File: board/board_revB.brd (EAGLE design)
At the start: 94 x 44.5 mm, 84 parts, among them Q1 ULN2003AS, Q2 ULN2003AD, Y1 8Mhz

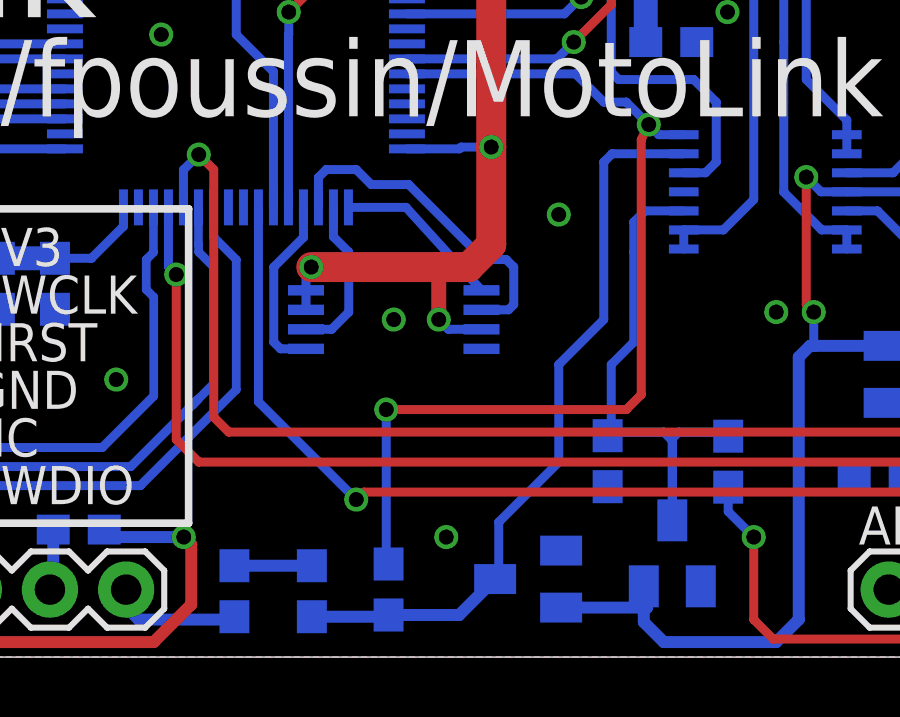
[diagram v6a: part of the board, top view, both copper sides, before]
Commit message: [GUI] Working on XML file saving
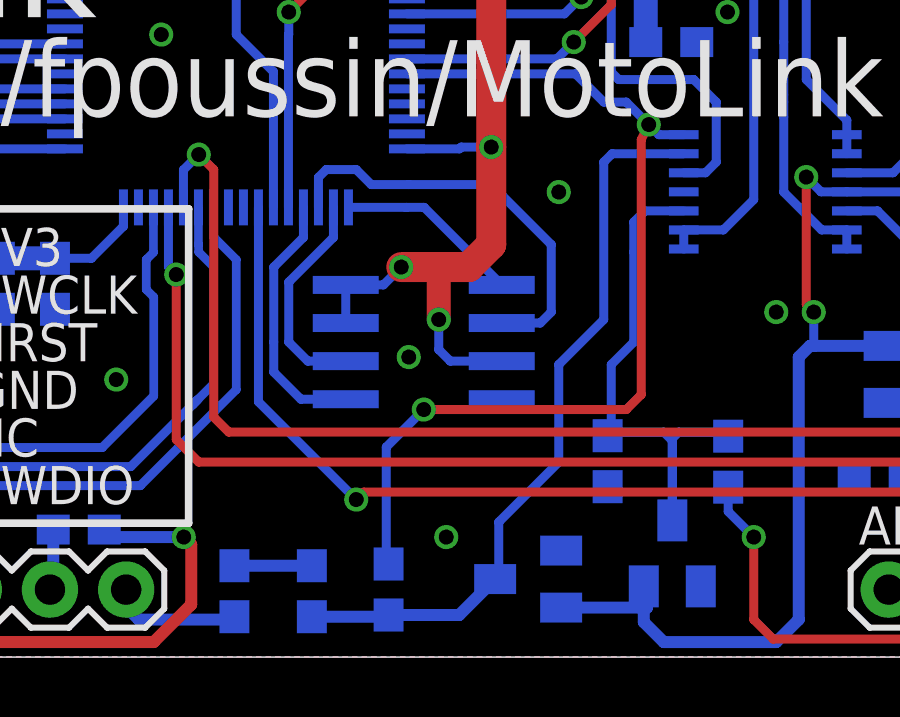
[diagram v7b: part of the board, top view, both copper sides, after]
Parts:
- IC_EE: value 25LC040ST -> 25LC080SN; device microchip:TSSOP8 -> microchip:SO-08
- moved IC_EE 1.25 mm to (48.5, 10.5)
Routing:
- net SPI2_MOSI: track 6.07 -> 8.67 mm
- net SPI2_MISO: track 11.4 -> 14.0 mm
- net SPI2_SCK: track 5.36 -> 7.27 mm
- net AN_KNOCK: track 33.0 -> 32.3 mm
- net +3V3: track 360.5 -> 361.1 mm
- net SPI2_NSS: track 5.66 -> 6.18 mm
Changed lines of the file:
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@@
 <?xml version="1.0" encoding="utf-8"?>
 <!DOCTYPE eagle SYSTEM "eagle.dtd">
-<eagle version="7.0.0">
+<eagle version="7.1.0">
 <drawing>
 <settings>
@@
 <attribute name="VALUE" x="84.75" y="38.025" size="1.016" layer="28" rot="MR0"/>
 </element>
-<element name="IC_EE" library="microchip" package="TSSOP8" value="25LC040ST" x="47.5" y="11.25" smashed="yes" rot="MR270">
-<attribute name="OC_NEWARK" value="72J3684" x="47.5" y="11.25" size="1.778" layer="28" font="vector" ratio="15" rot="MR270" display="off"/>
-<attribute name="MPN" value="25LC040A-I/ST" x="47.5" y="11.25" size="1.778" layer="28" font="vector" ratio="15" rot="MR270" display="off"/>
-<attribute name="MF" value="MICROCHIP" x="47.5" y="11.25" size="1.778" layer="28" font="vector" ratio="15" rot="MR270" display="off"/>
-<attribute name="OC_FARNELL" value="1815998" x="47.5" y="11.25" size="1.778" layer="28" font="vector" ratio="15" rot="MR270" display="off"/>
-<attribute name="NAME" x="50.425" y="12.875" size="1.27" layer="26" font="vector" ratio="16" rot="MR0"/>
-<attribute name="VALUE" x="50.75" y="8.325" size="1.27" layer="28" rot="MR0"/>
+<element name="IC_EE" library="microchip" package="SO-08" value="25LC080SN" x="48.5" y="10.5" smashed="yes" rot="MR270">
+<attribute name="OC_NEWARK" value="96K4092" x="48.5" y="10.5" size="1.778" layer="28" rot="MR270" display="off"/>
+<attribute name="MPN" value="25LC080/SN" x="48.5" y="10.5" size="1.778" layer="28" rot="MR270" display="off"/>
+<attribute name="MF" value="MICROCHIP" x="48.5" y="10.5" size="1.778" layer="28" rot="MR270" display="off"/>
+<attribute name="OC_FARNELL" value="1137302" x="48.5" y="10.5" size="1.778" layer="28" rot="MR270" display="off"/>
+<attribute name="NAME" x="51.405" y="13.417" size="1.27" layer="26" font="vector" ratio="16" rot="MR0"/>
+<attribute name="VALUE" x="50.405" y="6.563" size="1.27" layer="28" rot="MR0"/>
 </element>
 </elements>
@@
 <contactref element="C6" pad="2"/>
 <contactref element="C8" pad="1"/>
-<via x="53" y="14.75" extent="1-16" drill="0.5"/>
+<via x="53" y="15.5" extent="1-16" drill="0.5"/>
 <via x="39.75" y="20.75" extent="1-16" drill="0.5"/>
 <via x="11.5" y="39.5" extent="1-16" drill="0.5"/>
 <via x="19" y="6" extent="1-16" drill="0.5"/>
 <via x="38.25" y="9.25" extent="1-16" drill="0.5"/>
-<via x="47.5" y="11.25" extent="1-16" drill="0.5"/>
+<via x="48" y="10" extent="1-16" drill="0.5"/>
 <via x="60.25" y="11.5" extent="1-16" drill="0.5"/>
 <via x="82.75" y="3.5" extent="1-16" drill="0.5"/>
@@
 <via x="58.625" y="21.5" extent="1-16" drill="0.5"/>
 <contactref element="CON_USB" pad="4"/>
-<contactref element="IC_EE" pad="4"/>
 <via x="1.75" y="24.5" extent="1-16" drill="0.5"/>
 <via x="1" y="16.5" extent="1-16" drill="0.5"/>
 <via x="4.25" y="33.25" extent="1-16" drill="0.5"/>
+<contactref element="IC_EE" pad="4"/>
 </signal>
 <signal name="+3V3">
@@
 <wire x1="92.5" y1="26" x2="90.4525" y2="26" width="0.4" layer="16"/>
 <wire x1="90.4525" y1="26" x2="90.17" y2="25.7175" width="0.4" layer="16"/>
-<contactref element="IC_EE" pad="8"/>
 <wire x1="50.9" y1="16.85" x2="50.75" y2="17" width="0.3" layer="16"/>
-<wire x1="44.575" y1="12.225" x2="44.575" y2="12.825" width="0.3" layer="16"/>
-<wire x1="44.575" y1="12.825" x2="44.75" y2="13" width="0.3" layer="16"/>
-<via x="44.75" y="13" extent="1-16" drill="0.5"/>
+<via x="47.75" y="13" extent="1-16" drill="0.5"/>
 <wire x1="50.75" y1="17" x2="50.75" y2="13.75" width="1" layer="1"/>
 <wire x1="50.75" y1="13.75" x2="50" y2="13" width="1" layer="1"/>
 <wire x1="50" y1="13" x2="49" y2="13" width="1" layer="1"/>
+<wire x1="49" y1="13" x2="47.75" y2="13" width="1" layer="1"/>
+<via x="49" y="11.25" extent="1-16" drill="0.5"/>
+<wire x1="49" y1="11.25" x2="49" y2="13" width="0.8" layer="1"/>
+<contactref element="IC_EE" pad="7"/>
+<contactref element="IC_EE" pad="8"/>
 <contactref element="IC_EE" pad="3"/>
-<wire x1="49" y1="13" x2="44.75" y2="13" width="1" layer="1"/>
-<wire x1="50.425" y1="10.925" x2="49.325" y2="10.925" width="0.3" layer="16"/>
-<wire x1="49.325" y1="10.925" x2="49" y2="11.25" width="0.3" layer="16"/>
-<via x="49" y="11.25" extent="1-16" drill="0.5"/>
-<wire x1="49" y1="11.25" x2="49" y2="13" width="0.5" layer="1"/>
-<contactref element="IC_EE" pad="7"/>
-<wire x1="44.575" y1="12.225" x2="44.575" y2="11.575" width="0.3" layer="16"/>
+<wire x1="45.9" y1="11.135" x2="45.9" y2="12.405" width="0.3" layer="16"/>
+<wire x1="51.1" y1="9.865" x2="49.385" y2="9.865" width="0.3" layer="16"/>
+<wire x1="49.385" y1="9.865" x2="49" y2="10.25" width="0.3" layer="16"/>
+<wire x1="49" y1="10.25" x2="49" y2="11.25" width="0.3" layer="16"/>
+<wire x1="45.9" y1="12.405" x2="47.155" y2="12.405" width="0.3" layer="16"/>
+<wire x1="47.155" y1="12.405" x2="47.75" y2="13" width="0.3" layer="16"/>
 </signal>
 <signal name="+12V">
@@
 <contactref element="R5" pad="1"/>
 <wire x1="47.25" y1="3.18" x2="47.3275" y2="3.1025" width="0.3" layer="16"/>
-<wire x1="47.25" y1="3.18" x2="47.25" y2="8.25" width="0.3" layer="16"/>
-<via x="47.25" y="8.25" extent="1-16" drill="0.5"/>
-<wire x1="47.25" y1="8.25" x2="55.25" y2="8.25" width="0.3" layer="1"/>
+<via x="48.5" y="8.25" extent="1-16" drill="0.5"/>
+<wire x1="48.5" y1="8.25" x2="55.25" y2="8.25" width="0.3" layer="1"/>
 <wire x1="55.25" y1="8.25" x2="55.75" y2="8.75" width="0.3" layer="1"/>
 <wire x1="55.75" y1="8.75" x2="55.75" y2="17.25" width="0.3" layer="1"/>
@@
 <wire x1="54.5" y1="18.5" x2="55.25" y2="18.5" width="0.3" layer="16"/>
 <wire x1="55.25" y1="18.5" x2="56" y2="17.75" width="0.3" layer="16"/>
+<wire x1="47.25" y1="3.18" x2="47.25" y2="7" width="0.3" layer="16"/>
+<wire x1="47.25" y1="7" x2="48.5" y2="8.25" width="0.3" layer="16"/>
 </signal>
 <signal name="FREQ2_IN">
@@
 <signal name="SPI2_MOSI">
 <contactref element="STM32" pad="36"/>
-<contactref element="IC_EE" pad="5"/>
 <wire x1="44.49" y1="14.99" x2="44.49" y2="13.99" width="0.3" layer="16"/>
 <wire x1="44.49" y1="13.99" x2="43.5" y2="13" width="0.3" layer="16"/>
 <wire x1="43.5" y1="13" x2="43.5" y2="10.5" width="0.3" layer="16"/>
-<wire x1="44.575" y1="10.275" x2="43.725" y2="10.275" width="0.3" layer="16"/>
-<wire x1="43.725" y1="10.275" x2="43.5" y2="10.5" width="0.3" layer="16"/>
+<contactref element="IC_EE" pad="5"/>
+<wire x1="45.9" y1="8.595" x2="44.405" y2="8.595" width="0.3" layer="16"/>
+<wire x1="44.405" y1="8.595" x2="43.5" y2="9.5" width="0.3" layer="16"/>
+<wire x1="43.5" y1="9.5" x2="43.5" y2="10.5" width="0.3" layer="16"/>
 </signal>
 <signal name="SPI2_MISO">
 <contactref element="STM32" pad="35"/>
-<contactref element="IC_EE" pad="2"/>
 <wire x1="44.99" y1="14.99" x2="44.99" y2="15.99" width="0.3" layer="16"/>
 <wire x1="44.99" y1="15.99" x2="45.25" y2="16.25" width="0.3" layer="16"/>
@@
 <wire x1="46.25" y1="16.25" x2="46.75" y2="15.75" width="0.3" layer="16"/>
 <wire x1="46.75" y1="15.75" x2="48" y2="15.75" width="0.3" layer="16"/>
-<wire x1="48" y1="15.75" x2="50.5" y2="13.25" width="0.3" layer="16"/>
-<wire x1="50.5" y1="13.25" x2="51.25" y2="13.25" width="0.3" layer="16"/>
-<wire x1="51.25" y1="13.25" x2="51.5" y2="13" width="0.3" layer="16"/>
-<wire x1="50.425" y1="11.575" x2="51.325" y2="11.575" width="0.3" layer="16"/>
-<wire x1="51.325" y1="11.575" x2="51.5" y2="11.75" width="0.3" layer="16"/>
-<wire x1="51.5" y1="11.75" x2="51.5" y2="13" width="0.3" layer="16"/>
+<contactref element="IC_EE" pad="2"/>
+<wire x1="48" y1="15.75" x2="50.75" y2="15.75" width="0.3" layer="16"/>
+<wire x1="50.75" y1="15.75" x2="52.75" y2="13.75" width="0.3" layer="16"/>
+<wire x1="51.1" y1="11.135" x2="52.385" y2="11.135" width="0.3" layer="16"/>
+<wire x1="52.385" y1="11.135" x2="52.75" y2="11.5" width="0.3" layer="16"/>
+<wire x1="52.75" y1="11.5" x2="52.75" y2="13.75" width="0.3" layer="16"/>
 </signal>
 <signal name="SPI2_SCK">
 <contactref element="STM32" pad="34"/>
 <contactref element="IC_EE" pad="6"/>
-<wire x1="45.49" y1="14.99" x2="45.49" y2="14.01" width="0.3" layer="16"/>
-<wire x1="45.49" y1="14.01" x2="46" y2="13.5" width="0.3" layer="16"/>
-<wire x1="46" y1="13.5" x2="46" y2="11.5" width="0.3" layer="16"/>
-<wire x1="44.575" y1="10.925" x2="45.425" y2="10.925" width="0.3" layer="16"/>
-<wire x1="45.425" y1="10.925" x2="46" y2="11.5" width="0.3" layer="16"/>
+<wire x1="45.9" y1="9.865" x2="44.635" y2="9.865" width="0.3" layer="16"/>
+<wire x1="44.635" y1="9.865" x2="44" y2="10.5" width="0.3" layer="16"/>
+<wire x1="44" y1="10.5" x2="44" y2="12.5" width="0.3" layer="16"/>
+<wire x1="45.49" y1="14.99" x2="45.49" y2="13.99" width="0.3" layer="16"/>
+<wire x1="45.49" y1="13.99" x2="44" y2="12.5" width="0.3" layer="16"/>
 </signal>
 <signal name="SPI2_NSS">
 <contactref element="STM32" pad="33"/>
+<wire x1="45.99" y1="14.99" x2="47.91" y2="14.99" width="0.3" layer="16"/>
 <contactref element="IC_EE" pad="1"/>
-<wire x1="45.99" y1="14.99" x2="47.91" y2="14.99" width="0.3" layer="16"/>
-<wire x1="47.91" y1="14.99" x2="50.425" y2="12.225" width="0.3" layer="16"/>
+<wire x1="47.91" y1="14.99" x2="48.515" y2="14.99" width="0.3" layer="16"/>
+<wire x1="48.515" y1="14.99" x2="51.1" y2="12.405" width="0.3" layer="16"/>
 </signal>
 </signals>

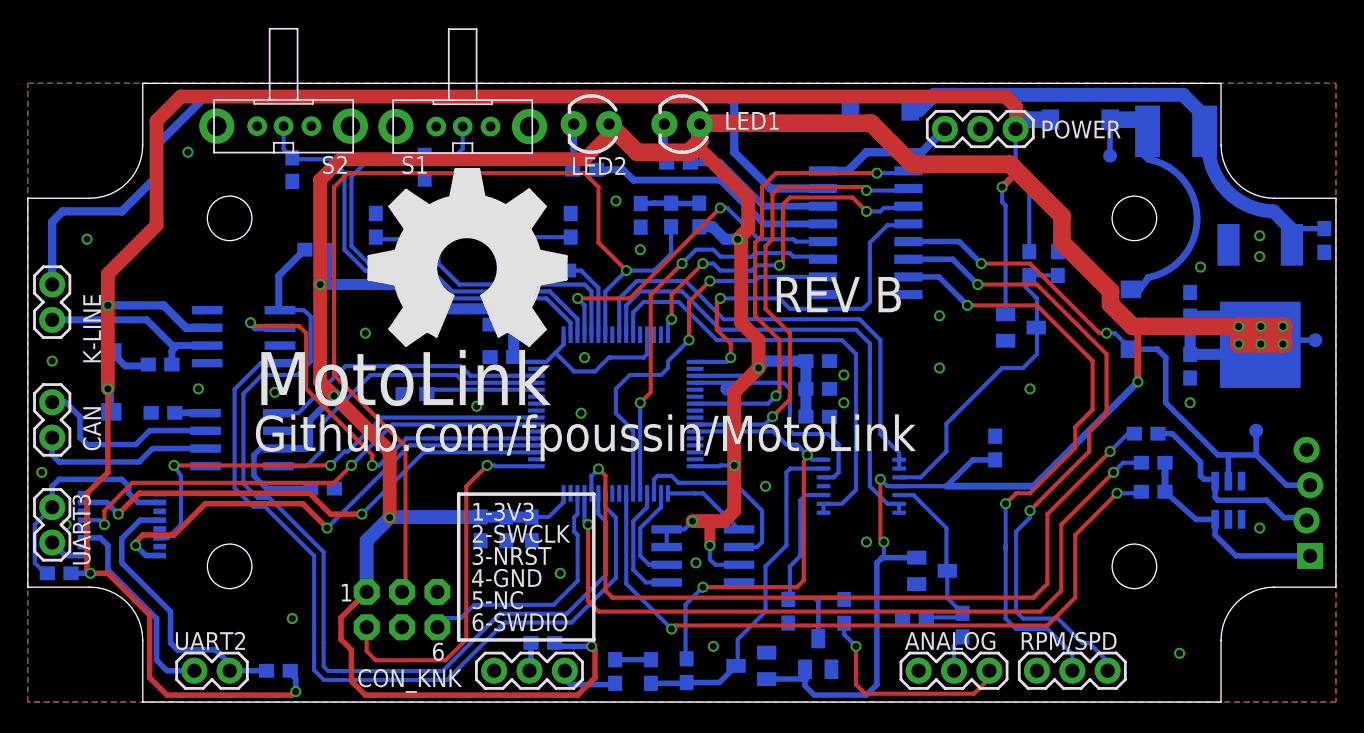
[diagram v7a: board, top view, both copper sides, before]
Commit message: [GUI/Code] Rewrote DSP functions, switched to float; Updated DSP library
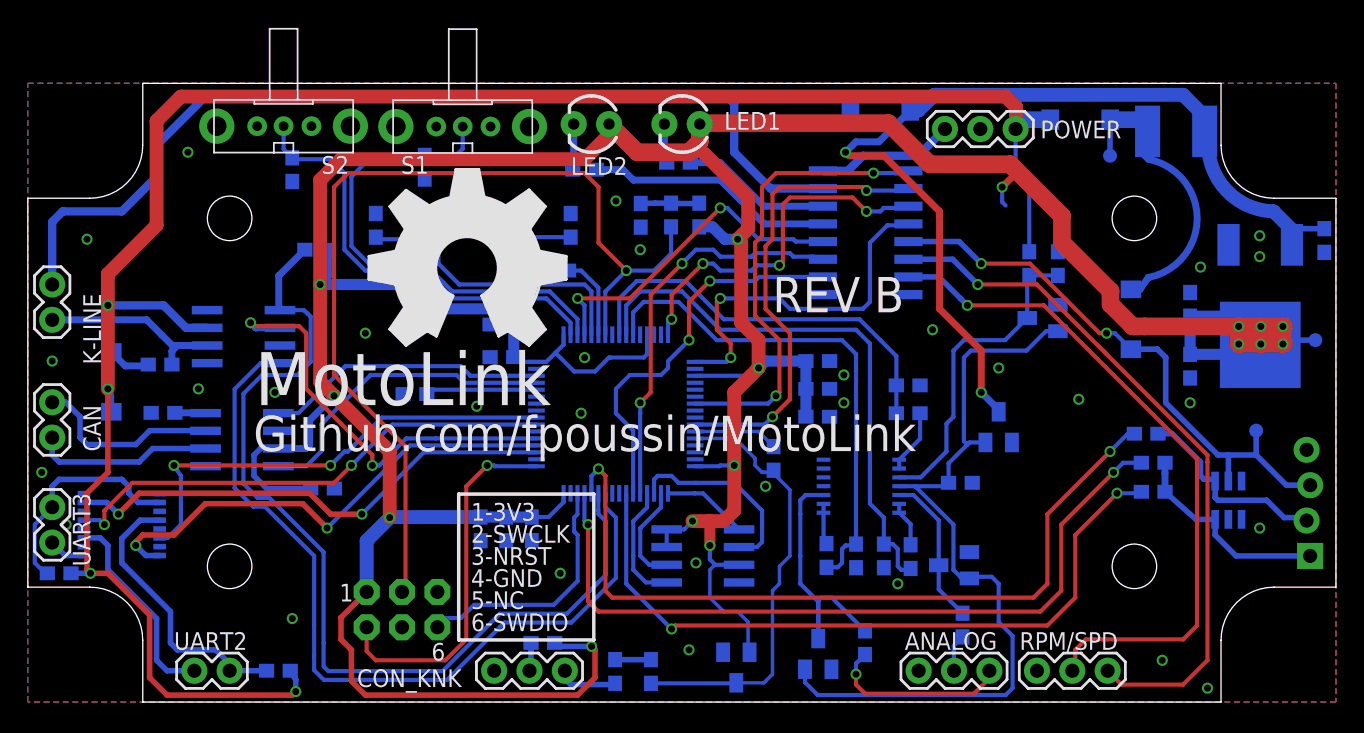
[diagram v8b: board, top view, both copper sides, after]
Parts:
- removed TP1: (no value), microbuilder:TESTPOINT_ROUND_1MM
- added IC1: MCP1703CB, linear:SOT23
- added R19, R20, R23, R24: 10K 1%, SparkFun-Resistors:0603-RES
- IC_OPA: value MCP6004 -> TL974IPW
- R30: value 100K -> 100K 1%
- R31: value 10K -> 10K 1%
- R32, R4: value 1M -> 100K
- R6, R7: value 1M -> 10K 1%
- moved R5 16.5 mm to (53.6, 17.5)
- moved R6 4.85 mm to (57.4, 10.5)
- moved R7 4.38 mm to (63.4, 10.4), turned to 90 degrees
- moved C6 3.54 mm to (67.0, 15.8), turned to 180 degrees
- moved R32 2.70 mm to (60.1, 4.26)
- moved D2 1.70 mm to (72.9, 27.6), turned to 270 degrees
- moved D3 1.63 mm to (66.5, 9.83), turned to 270 degrees
- moved D4 1.09 mm to (50.9, 2.48), turned to 180 degrees
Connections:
- removed net AN_KNOCK: IC_OPA.14, R5.1, STM32.27
- removed net N$12: D4.3, IC_OPA.13, R5.2, R8.1
- removed net N$20: C1.1, F1.1, IC_REG.3, TVS1.C
- new net +5V: C6.1, D2.2, D3.2, D7.2, IC1.2, IC_OPA.4
- new net AN1_N: IC_OPA.1, IC_OPA.2, R23.1
- new net AN2_N: IC_OPA.8, IC_OPA.9, R6.2
- new net AN3_N: IC_OPA.6, IC_OPA.7, R7.2
- new net DAC2: STM32.21
- new net OP3_VINM: D4.3, R5.2, R8.1, STM32.28
- new net OP3_VOUT: R5.1, STM32.27
- new net VCC_PROT: C1.1, F1.1, IC1.3, IC_REG.3, TVS1.C
- net +3V3: no longer C6.1, D2.2, D3.2, D7.2, IC_OPA.4
- net AN1: now also R23.2, R24.2; no longer IC_OPA.1, IC_OPA.2
- net AN2: now also R19.1, R6.1; no longer IC_OPA.8, IC_OPA.9
- net AN3: now also R20.1, R7.1; no longer IC_OPA.6, IC_OPA.7
- net DAC1: no longer IC_OPA.12, TP1.P$1
- net GND: now also IC1.1, R19.2, R20.2, R24.1; no longer R6.1, R7.1
- net N$25: no longer R6.2
- net N$5: no longer R7.2
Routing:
- net VCC_PROT: track 0.00 -> 67.1 mm, vias 0 -> 2
- net +5V: track 0.00 -> 58.1 mm
- net +3V3: track 361.1 -> 305.6 mm, vias 19 -> 16
- net N$20: track 36.3 -> 0.00 mm
- net OP3_VINM: track 0.00 -> 32.3 mm
- net AN_KNOCK: track 32.3 -> 0.00 mm, vias 2 -> 0
- net N$12: track 24.8 -> 0.00 mm
- net DAC1: track 17.7 -> 0.00 mm
- net OP3_VOUT: track 0.00 -> 6.09 mm
- net AN3: track 35.1 -> 39.9 mm
- net AN1_N: track 0.00 -> 4.59 mm
- net N$21: track 44.7 -> 49.2 mm, vias 2 -> 1
- net N$16: track 47.0 -> 51.3 mm, vias 2 -> 1
- net AN1: track 33.4 -> 29.4 mm
- net AN2: track 32.6 -> 36.5 mm
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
